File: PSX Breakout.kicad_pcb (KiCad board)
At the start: 2 copper layers, 100 x 44.9 mm, 15 parts, among them J1 Conn_01x12_Male, J2 Mini-DIN-4, J3 AudioJack3, J4 DB15_Female_HighDensity, J5 3x2_RCA, SW1 SW_SPDT

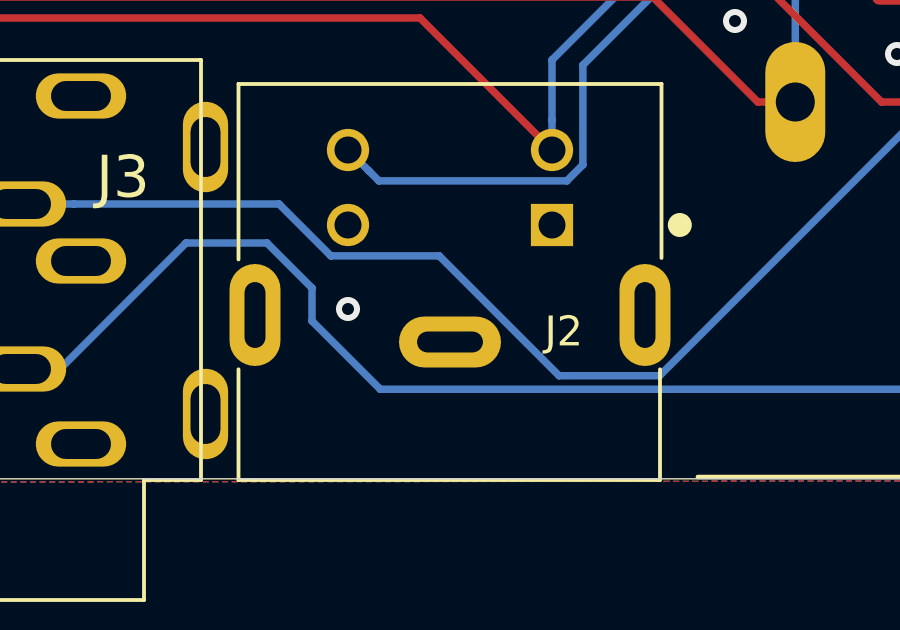
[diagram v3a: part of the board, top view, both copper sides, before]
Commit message: Changed s-video footprint
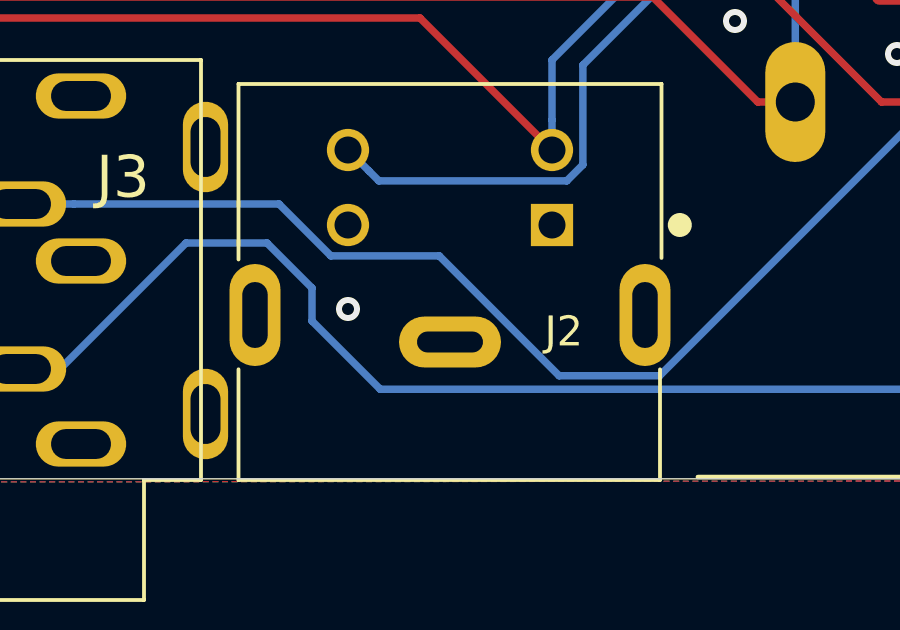
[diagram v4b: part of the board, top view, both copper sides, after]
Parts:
- J2: footprint MD-40SG:CUI_MD-40SG -> Tinkerplunk:CUI_MD-40SG
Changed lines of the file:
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@@
     (add_net VGA_SYNC_OUT)
+  )
+  (module Tinkerplunk:CUI_MD-40SG (layer F.Cu)
+    (at 141.4 98.3 180)
+    (fp_text reference J2 (at -3.7925 -1.651 180) (layer F.SilkS)
+      (effects (font (size 1 1) (thickness 0.15)))
+    )
+    (fp_text value Mini-DIN-4 (at -0.127 8.001 180) (layer F.SilkS) hide
+      (effects (font (size 1.00063 1.00063) (thickness 0.05)))
+    )
+    (fp_circle (center -5.12 1.9) (end -4.92 1.9) (layer Eco2.User) (width 0.4))
+    (fp_circle (center -7.66 1.9) (end -7.46 1.9) (layer F.SilkS) (width 0.4))
+    (fp_line (start 5.25 -6.6) (end 4.89 -6.6) (layer Eco2.User) (width 0.127))
+    (fp_line (start 7.05 6.6) (end 7.05 0.75) (layer F.SilkS) (width 0.127))
+    (fp_line (start 7.05 -6.6) (end 7.05 -2.91) (layer F.SilkS) (width 0.127))
+    (fp_line (start -7.05 6.6) (end -7.05 0.8) (layer F.SilkS) (width 0.127))
+    (fp_line (start -7 -6.6) (end -7 -2.91) (layer F.SilkS) (width 0.127))
+    (fp_line (start -7.25 -6.95) (end -7.25 -2.8) (layer Eco1.User) (width 0.05))
+    (fp_line (start -7.85 -2.8) (end -7.25 -2.8) (layer Eco1.User) (width 0.05))
+    (fp_line (start -7.85 0.6) (end -7.85 -2.8) (layer Eco1.User) (width 0.05))
+    (fp_line (start -7.25 0.6) (end -7.85 0.6) (layer Eco1.User) (width 0.05))
+    (fp_line (start -7.25 6.85) (end -7.25 0.6) (layer Eco1.User) (width 0.05))
+    (fp_line (start 7.3 6.85) (end -7.25 6.85) (layer Eco1.User) (width 0.05))
+    (fp_line (start 7.3 0.6) (end 7.3 6.85) (layer Eco1.User) (width 0.05))
+    (fp_line (start 7.8 0.6) (end 7.3 0.6) (layer Eco1.User) (width 0.05))
+    (fp_line (start 7.8 -2.8) (end 7.8 0.6) (layer Eco1.User) (width 0.05))
+    (fp_line (start 7.25 -2.8) (end 7.8 -2.8) (layer Eco1.User) (width 0.05))
+    (fp_line (start 7.25 -6.95) (end 7.25 -2.8) (layer Eco1.User) (width 0.05))
+    (fp_line (start -7.25 -6.95) (end 7.25 -6.95) (layer Eco1.User) (width 0.05))
+    (fp_line (start 7.05 6.6) (end -7.05 6.6) (layer Eco2.User) (width 0.127))
+    (fp_line (start 7.05 -6.6) (end 7.05 6.6) (layer Eco2.User) (width 0.127))
+    (fp_line (start 5.25 -6.6) (end 7.05 -6.6) (layer Eco2.User) (width 0.127))
+    (fp_line (start 4.89 -6.6) (end 5.25 -6.6) (layer Eco2.User) (width 0.127))
+    (fp_line (start -7.05 -6.6) (end 4.89 -6.6) (layer Eco2.User) (width 0.127))
+    (fp_line (start -7.05 6.6) (end -7.05 -6.6) (layer Eco2.User) (width 0.127))
+    (fp_line (start 7.05 6.6) (end -7.05 6.6) (layer F.SilkS) (width 0.127))
+    (fp_line (start -7 -6.6) (end 7.05 -6.6) (layer F.SilkS) (width 0.127))
+    (pad 4 thru_hole circle (at 3.4 4.4 90) (size 1.408 1.408) (drill 0.9) (layers *.Cu *.Mask)
+      (net 13 CHROMA))
+    (pad 2 thru_hole circle (at 3.4 1.9 90) (size 1.408 1.408) (drill 0.9) (layers *.Cu *.Mask)
+      (net 7 GND))
+    (pad 1 thru_hole rect (at -3.4 1.9 90) (size 1.408 1.408) (drill 0.9) (layers *.Cu *.Mask)
+      (net 7 GND))
+    (pad 3 thru_hole circle (at -3.4 4.4 90) (size 1.408 1.408) (drill 0.9) (layers *.Cu *.Mask)
+      (net 11 LUMA))
+    (pad S3 thru_hole oval (at 6.5 -1.1 90) (size 3.4 1.7) (drill oval 2.2 0.85) (layers *.Cu *.Mask))
+    (pad S2 thru_hole oval (at 0 -2) (size 3.4 1.7) (drill oval 2.2 0.7) (layers *.Cu *.Mask))
+    (pad S1 thru_hole oval (at -6.5 -1.1 270) (size 3.4 1.7) (drill oval 2.2 0.85) (layers *.Cu *.Mask))
+    (model ${KIPRJMOD}/PSX_BREAKOUT.Pretty/CUI_MD-40SM.step
+      (offset (xyz 0 6.5 6.5))
+      (scale (xyz 1 1 1))
+      (rotate (xyz -90 0 -90))
+    )
   )
   (module MountingHole:MountingHole_5.5mm (layer F.Cu)
@@
     )
   )
-  (module MD-40SG:CUI_MD-40SG (layer F.Cu)
-    (at 141.4 98.3 180)
-    (fp_text reference J2 (at -3.7925 -1.651 180) (layer F.SilkS)
-      (effects (font (size 1 1) (thickness 0.15)))
-    )
-    (fp_text value Mini-DIN-4 (at -0.127 8.001 180) (layer F.SilkS) hide
-      (effects (font (size 1.00063 1.00063) (thickness 0.05)))
-    )
-    (fp_line (start -7 -6.6) (end 7.05 -6.6) (layer F.SilkS) (width 0.127))
-    (fp_line (start 7.05 6.6) (end -7.05 6.6) (layer F.SilkS) (width 0.127))
-    (fp_line (start -7.05 6.6) (end -7.05 -6.6) (layer Eco2.User) (width 0.127))
-    (fp_line (start -7.05 -6.6) (end 4.89 -6.6) (layer Eco2.User) (width 0.127))
-    (fp_line (start 4.89 -6.6) (end 5.25 -6.6) (layer Eco2.User) (width 0.127))
-    (fp_line (start 5.25 -6.6) (end 7.05 -6.6) (layer Eco2.User) (width 0.127))
-    (fp_line (start 7.05 -6.6) (end 7.05 6.6) (layer Eco2.User) (width 0.127))
-    (fp_line (start 7.05 6.6) (end -7.05 6.6) (layer Eco2.User) (width 0.127))
-    (fp_line (start -7.25 -6.95) (end 7.25 -6.95) (layer Eco1.User) (width 0.05))
-    (fp_line (start 7.25 -6.95) (end 7.25 -2.8) (layer Eco1.User) (width 0.05))
-    (fp_line (start 7.25 -2.8) (end 7.8 -2.8) (layer Eco1.User) (width 0.05))
-    (fp_line (start 7.8 -2.8) (end 7.8 0.6) (layer Eco1.User) (width 0.05))
-    (fp_line (start 7.8 0.6) (end 7.3 0.6) (layer Eco1.User) (width 0.05))
-    (fp_line (start 7.3 0.6) (end 7.3 6.85) (layer Eco1.User) (width 0.05))
-    (fp_line (start 7.3 6.85) (end -7.25 6.85) (layer Eco1.User) (width 0.05))
-    (fp_line (start -7.25 6.85) (end -7.25 0.6) (layer Eco1.User) (width 0.05))
-    (fp_line (start -7.25 0.6) (end -7.85 0.6) (layer Eco1.User) (width 0.05))
-    (fp_line (start -7.85 0.6) (end -7.85 -2.8) (layer Eco1.User) (width 0.05))
-    (fp_line (start -7.85 -2.8) (end -7.25 -2.8) (layer Eco1.User) (width 0.05))
-    (fp_line (start -7.25 -6.95) (end -7.25 -2.8) (layer Eco1.User) (width 0.05))
-    (fp_line (start -7 -6.6) (end -7 -2.91) (layer F.SilkS) (width 0.127))
-    (fp_line (start -7.05 6.6) (end -7.05 0.8) (layer F.SilkS) (width 0.127))
-    (fp_line (start 7.05 -6.6) (end 7.05 -2.91) (layer F.SilkS) (width 0.127))
-    (fp_line (start 7.05 6.6) (end 7.05 0.75) (layer F.SilkS) (width 0.127))
-    (fp_line (start 5.25 -6.6) (end 4.89 -6.6) (layer Eco2.User) (width 0.127))
-    (fp_circle (center -7.66 1.9) (end -7.46 1.9) (layer F.SilkS) (width 0.4))
-    (fp_circle (center -5.12 1.9) (end -4.92 1.9) (layer Eco2.User) (width 0.4))
-    (pad S1 thru_hole oval (at -6.5 -1.1 270) (size 3.4 1.7) (drill oval 2.2 0.7) (layers *.Cu *.Mask))
-    (pad S2 thru_hole oval (at 0 -2) (size 3.4 1.7) (drill oval 2.2 0.7) (layers *.Cu *.Mask))
-    (pad S3 thru_hole oval (at 6.5 -1.1 90) (size 3.4 1.7) (drill oval 2.2 0.7) (layers *.Cu *.Mask))
-    (pad 3 thru_hole circle (at -3.4 4.4 90) (size 1.408 1.408) (drill 0.9) (layers *.Cu *.Mask)
-      (net 11 LUMA))
-    (pad 1 thru_hole rect (at -3.4 1.9 90) (size 1.408 1.408) (drill 0.9) (layers *.Cu *.Mask)
-      (net 7 GND))
-    (pad 2 thru_hole circle (at 3.4 1.9 90) (size 1.408 1.408) (drill 0.9) (layers *.Cu *.Mask)
-      (net 7 GND))
-    (pad 4 thru_hole circle (at 3.4 4.4 90) (size 1.408 1.408) (drill 0.9) (layers *.Cu *.Mask)
-      (net 13 CHROMA))
-    (model ${KIPRJMOD}/PSX_BREAKOUT.Pretty/CUI_MD-40SM.step
-      (offset (xyz 0 6.5 6.5))
-      (scale (xyz 1 1 1))
-      (rotate (xyz -90 0 -90))
-    )
-  )

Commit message: Finishing Touches
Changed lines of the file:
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@@
   (via (at 135.1 81) (size 0.8) (drill 0.4) (layers F.Cu B.Cu) (net 7))
   (via (at 130.2 80.9) (size 0.8) (drill 0.4) (layers F.Cu B.Cu) (net 7))
-  (via (at 120 80.9) (size 0.8) (drill 0.4) (layers F.Cu B.Cu) (net 7))
-  (via (at 115 80.9) (size 0.8) (drill 0.4) (layers F.Cu B.Cu) (net 7))
+  (via (at 120 82.4) (size 0.8) (drill 0.4) (layers F.Cu B.Cu) (net 7))
+  (via (at 115.1 84.6) (size 0.8) (drill 0.4) (layers F.Cu B.Cu) (net 7))
   (via (at 108.5 80.1) (size 0.8) (drill 0.4) (layers F.Cu B.Cu) (net 7))
   (via (at 96.1 87.1) (size 0.8) (drill 0.4) (layers F.Cu B.Cu) (net 7))
@@
       )
     )
+  )
+  (zone (net 0) (net_name "") (layer B.Mask) (hatch edge 0.508)
+    (connect_pads (clearance 0.508))
+    (min_thickness 0.254)
+    (fill yes (arc_segments 32) (thermal_gap 0.508) (thermal_bridge_width 0.508))
+    (polygon
+      (pts
+        (xy 124.8 81.3) (xy 124.8 76) (xy 114.2 76) (xy 114.2 81.3)
+      )
+    )
